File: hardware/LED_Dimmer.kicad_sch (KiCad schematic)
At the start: 20 parts, among them J1 Molex PicoBlade 53261-0871 1x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, J2 PicoBlade_510210800_1x08, M1 500798001, M2 500798001, M3 500798001, M4 500798001, M5 500798001, M6 500798001, M7 500798001, M8 500798001, Q1 2N7002K-7, Q2 2N7002K-7, Q3 2N7002K-7, U1 BGM220P, U2 L78L33A

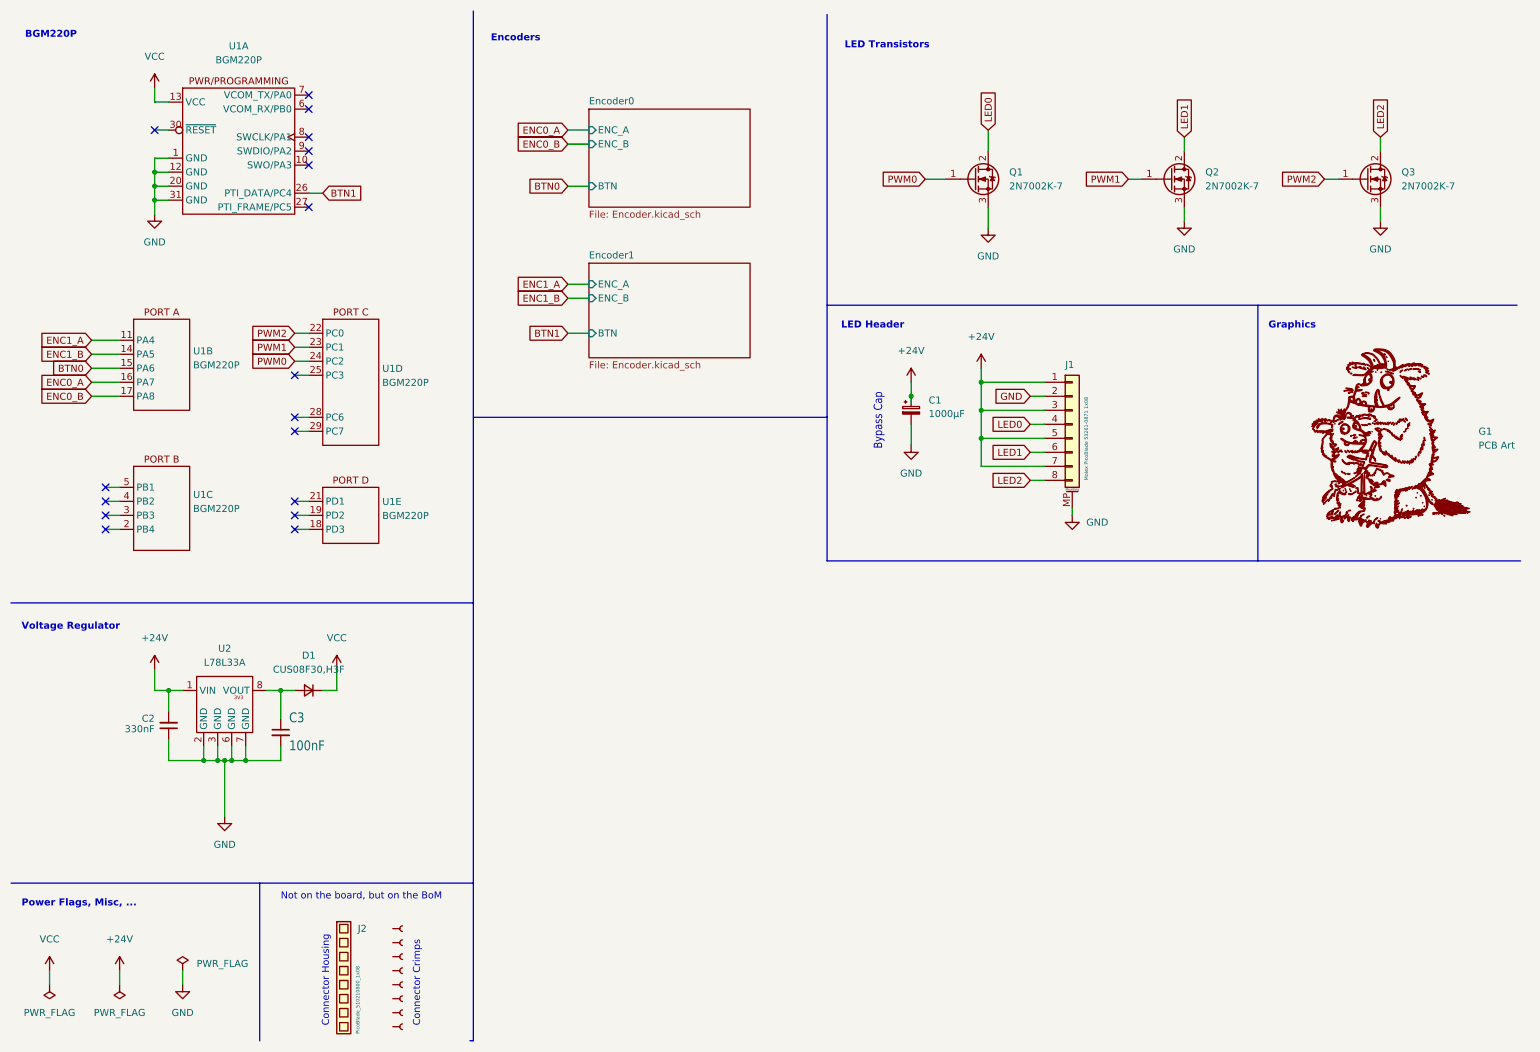
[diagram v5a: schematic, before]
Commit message: Updated to KiCad 9
- Changed LED Connectors to Kyocera
- Made board bigger
- Made art better and bigger
- Micro breakout now has header pins outside (easier to solder)
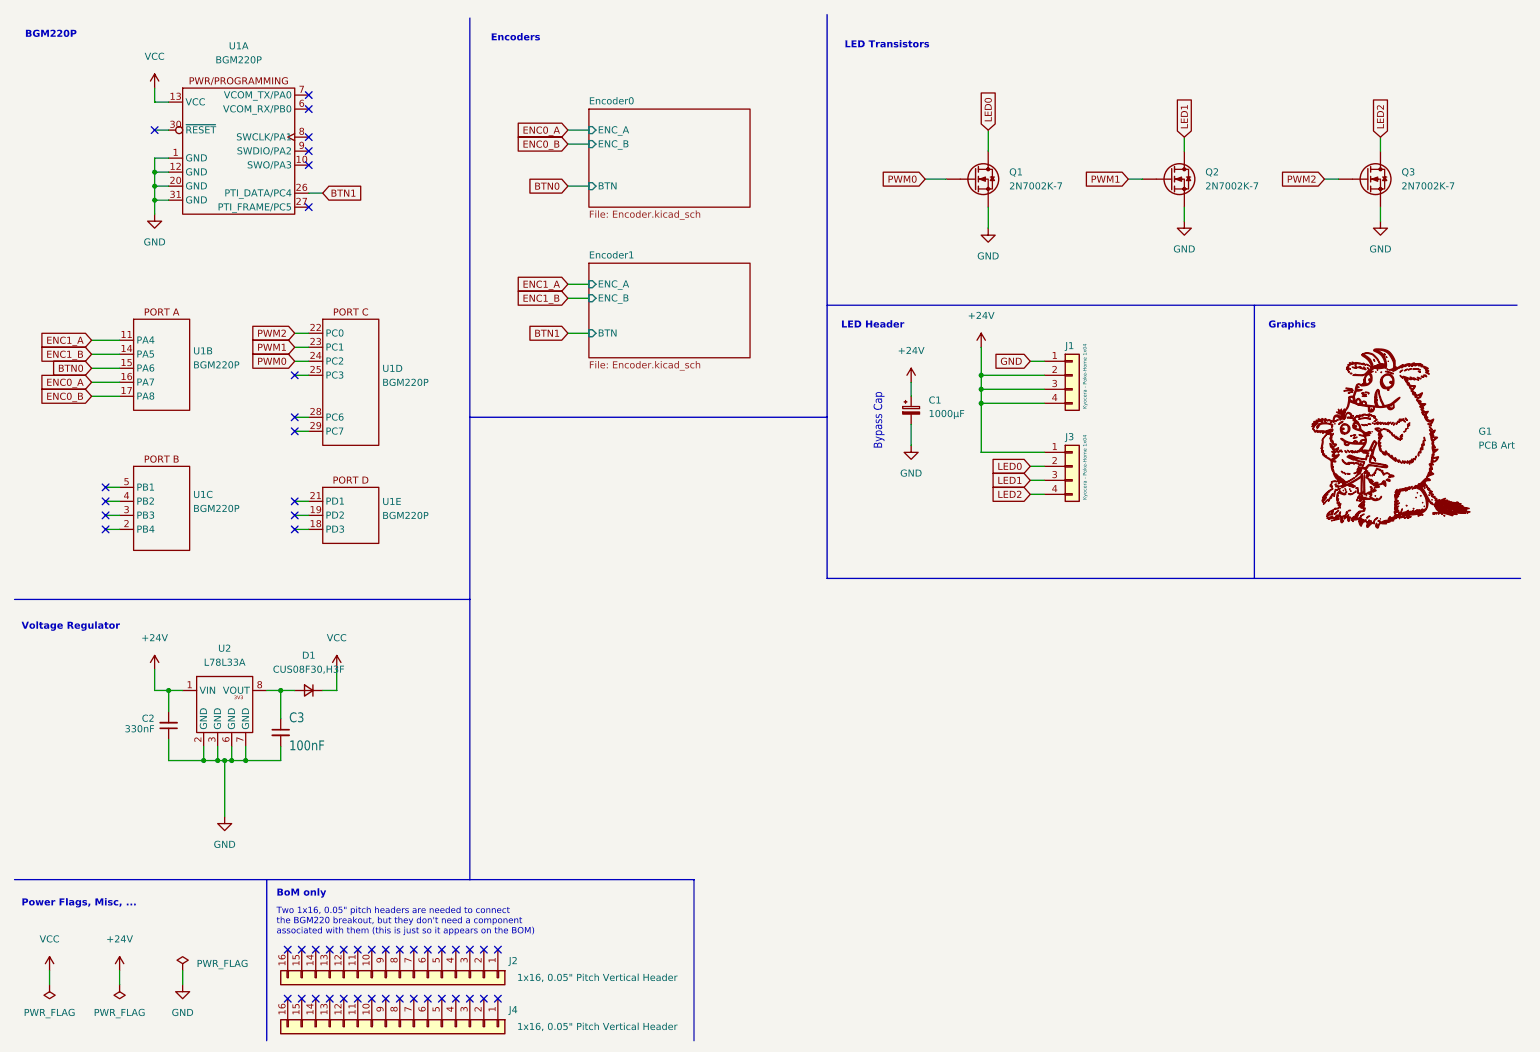
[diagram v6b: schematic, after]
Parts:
- removed J2: PicoBlade_510210800_1x08, symbol Gruffalo_Dimmer:PicoBlade_Housing_510210800_1x08
- removed M1, M2, M3, M4, M5, M6, M7, M8: 500798001, symbol Gruffalo_Dimmer:PicoBlade_Crimp_500798001_1x01
- added J2, J4: 1x16, 0.05" Pitch Vertical Header, symbol Connector_Generic:Conn_01x16
- added J3: Kyocera - Poke-Home 1x04, Gruffalo_Dimmer:Connector - Kyocera - Poke-Home 1x04 – Standard Horizontal 18-26 AWG, symbol Connector_Generic:Conn_01x04
- G1: footprint Gruffalo_Dimmer:Gruffalo_Art -> Gruffalo_Dimmer:Gruffalo_Art_42x47mm
- J1: value Molex PicoBlade 53261-0871 1x08 -> Kyocera - Poke-Home 1x04; footprint Gruffalo_Dimmer:Receptacle - Molex PicoBlade - SMD Right Angle 1x08 -> Gruffalo_Dimmer:Connector - Kyocera - Poke-Home 1x04 – Standard Horizontal 18-26 AWG; symbol Connector_Generic_MountingPin:Conn_01x08_MountingPin -> Connector_Generic:Conn_01x04; Comments Molex PicoBlade 1x08, SMD, Right Angle. Mates with P/N 5102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 -> Kyocera - Poke-Home 1x04 – Standard Horizontal 18-26 AWG; Digikey PN WM7626CT-ND -> (none); Farnell PN 1125376 -> (none); MPN 532610871 -> (none)
- Q1, Q2, Q3: symbol Device:Q_NMOS_GDS -> Device:Q_NMOS
- U1: footprint BGM220P_Breakout:BGM220P_Header_SMD -> BGM220P_Breakout:BGM220P_Header_SMD_Out
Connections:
- net +24V: now also J1.2 (Pin_2), J1.4 (Pin_4), J3.1 (Pin_1); no longer J1.1 (Pin_1), J1.5 (Pin_5), J1.7 (Pin_7)
- net GND: now also J1.1 (Pin_1), Q1.S, Q2.S, Q3.S; no longer J1.2 (Pin_2), J1.MP (MountPin), Q1.3 (S), Q2.3 (S), Q3.3 (S)
- net LED0: now also Q1.D, J3.2 (Pin_2); no longer J1.4 (Pin_4), Q1.2 (D)
- net LED1: now also Q2.D, J3.3 (Pin_3); no longer J1.6 (Pin_6), Q2.2 (D)
- net LED2: now also Q3.D, J3.4 (Pin_4); no longer J1.8 (Pin_8), Q3.2 (D)
- net PWM0: now also Q1.G; no longer Q1.1 (G)
- net PWM1: now also Q2.G; no longer Q2.1 (G)
- net PWM2: now also Q3.G; no longer Q3.1 (G)
- no-connect marks 17 -> 49
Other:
- note added: "BoM only"
- note added: "Two 1x16, 0.05" pitch headers are needed to connect the BGM220 breakout, but they don't need a component associated with them (this is just so it appears on the BOM)"
- note removed: "Connector Crimps"
- note removed: "Connector Housing"
- note removed: "Not on the board, but on the BoM"

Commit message: KiBot Config Udpdated to KiCad9
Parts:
- G1, J2, J4: Digikey PN (none) -> -; Farnell PN (none) -> -; MPN (none) -> -; Manufacturer (none) -> -
- J1, J3: Digikey PN (none) -> 478-009276004021906CT-ND; Farnell PN (none) -> 1891140; MPN (none) -> 009276004021906; Manufacturer Molex -> Kyocera
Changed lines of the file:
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@@
+			)
+		)
+		(property "Digikey PN" "-"
+			(at 82.55 195.58 90)
+			(effects
+				(font
+					(size 1.27 1.27)
+				)
+				(hide yes)
+			)
+		)
+		(property "Farnell PN" "-"
+			(at 82.55 195.58 90)
+			(effects
+				(font
+					(size 1.27 1.27)
+				)
+				(hide yes)
+			)
+		)
+		(property "MPN" "-"
+			(at 82.55 195.58 90)
+			(effects
+				(font
+					(size 1.27 1.27)
+				)
+				(hide yes)
+			)
+		)
+		(property "Manufacturer" "-"
+			(at 82.55 195.58 90)
+			(effects
+				(font
+					(size 1.27 1.27)
+				)
+				(hide yes)
 			)
 		)
@@
 			)
 		)
-		(property "Datasheet" "~"
+		(property "Datasheet" "https://datasheets.kyocera-avx.com/PokeHomeHorizontal_00-9276.pdf"
 			(at 204.47 77.47 0)
 			(effects
@@
 			)
 		)
-		(property "Digikey PN" ""
+		(property "Digikey PN" "478-009276004021906CT-ND"
 			(at 204.47 77.47 0)
 			(effects
@@
 			)
 		)
-		(property "Farnell PN" ""
+		(property "Farnell PN" "1891140"
 			(at 204.47 77.47 0)
 			(effects
@@
 			)
 		)
-		(property "MPN" ""
+		(property "MPN" "009276004021906"
 			(at 204.47 77.47 0)
 			(effects
@@
 			)
 		)
-		(property "Manufacturer" "Molex"
+		(property "Manufacturer" "Kyocera"
 			(at 204.47 77.47 0)
 			(effects
@@
 			)
 		)
-		(property "Datasheet" "~"
+		(property "Datasheet" "https://datasheets.kyocera-avx.com/PokeHomeHorizontal_00-9276.pdf"
 			(at 204.47 93.98 0)
 			(effects
@@
 			)
 		)
-		(property "Digikey PN" ""
+		(property "Digikey PN" "478-009276004021906CT-ND"
 			(at 204.47 93.98 0)
 			(effects
@@
 			)
 		)
-		(property "Farnell PN" ""
+		(property "Farnell PN" "1891140"
 			(at 204.47 93.98 0)
 			(effects
@@
 			)
 		)
-		(property "MPN" ""
+		(property "MPN" "009276004021906"
 			(at 204.47 93.98 0)
 			(effects
@@
 			)
 		)
-		(property "Manufacturer" "Molex"
+		(property "Manufacturer" "Kyocera"
 			(at 204.47 93.98 0)
 			(effects
@@
 			)
 		)
+		(property "Digikey PN" "-"
+			(at 82.55 186.69 90)
+			(effects
+				(font
+					(size 1.27 1.27)
+				)
+				(hide yes)
+			)
+		)
+		(property "Farnell PN" "-"
+			(at 82.55 186.69 90)
+			(effects
+				(font
+					(size 1.27 1.27)
+				)
+				(hide yes)
+			)
+		)
+		(property "MPN" "-"
+			(at 82.55 186.69 90)
+			(effects
+				(font
+					(size 1.27 1.27)
+				)
+				(hide yes)
+			)
+		)
+		(property "Manufacturer" "-"
+			(at 82.55 186.69 90)
+			(effects
+				(font
+					(size 1.27 1.27)
+				)
+				(hide yes)
+			)
+		)
 		(pin "6"
 		)
@@
 			)
 		)
-		(property "Datasheet" ""
+		(property "Datasheet" "~"
 			(at 262.255 88.9 0)
 			(effects
@@
 			)
 		)
+		(property "Digikey PN" "-"
+			(at 262.255 88.9 0)
+			(effects
+				(font
+					(size 1.27 1.27)
+				)
+				(hide yes)
+			)
+		)
+		(property "Farnell PN" "-"
+			(at 262.255 88.9 0)
+			(effects
+				(font
+					(size 1.27 1.27)
+				)
+				(hide yes)
+			)
+		)
+		(property "MPN" "-"
+			(at 262.255 88.9 0)
+			(effects
+				(font
+					(size 1.27 1.27)
+				)
+				(hide yes)
+			)
+		)
+		(property "Manufacturer" "-"
+			(at 262.255 88.9 0)
+			(effects
+				(font
+					(size 1.27 1.27)
+				)
+				(hide yes)
+			)
+		)

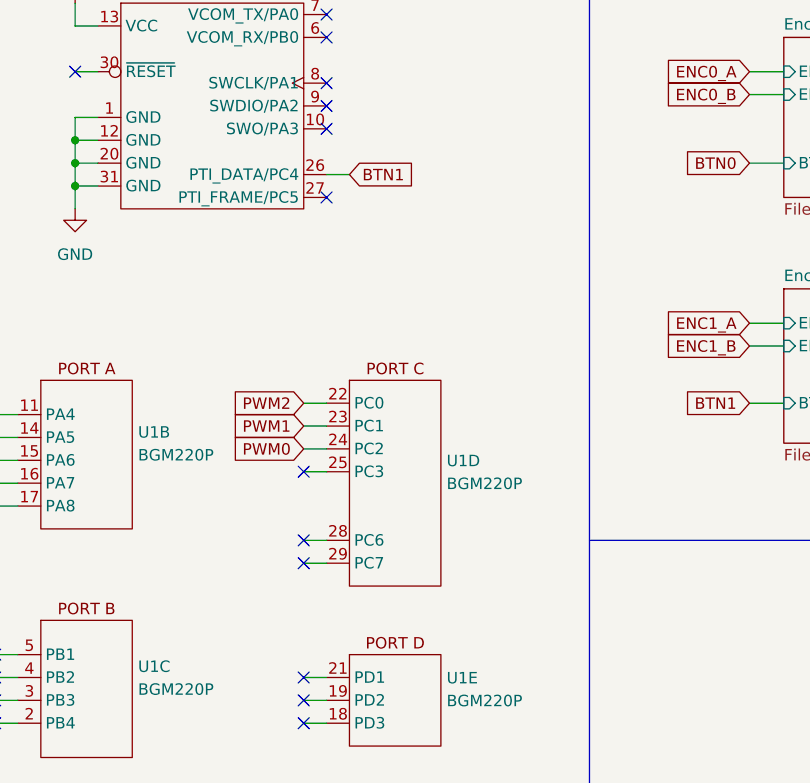
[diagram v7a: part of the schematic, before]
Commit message: Connected buttons to EM4 wake up pins
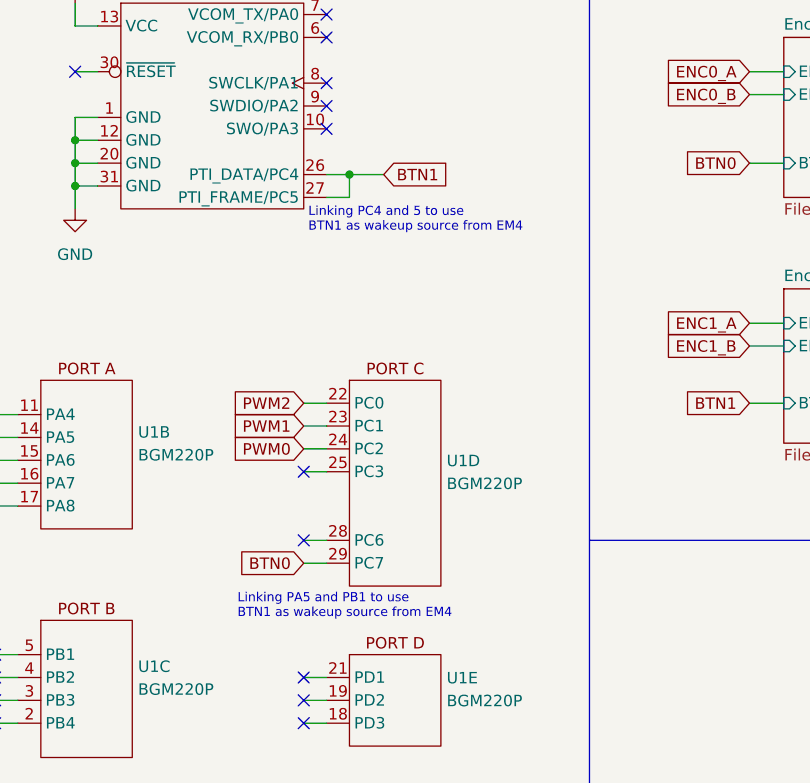
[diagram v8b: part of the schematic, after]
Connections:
- net BTN0: now also U1.29 (PC7)
- net BTN1: now also U1.27 (PTI_FRAME/PC5)
- no-connect marks 49 -> 47
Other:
- note added: "Linking PA5 and PB1 to use BTN1 as wakeup source from EM4"
- note added: "Linking PC4 and 5 to use BTN1 as wakeup source from EM4"
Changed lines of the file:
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@@
+		)
+	)
+	(text "Linking PC4 and 5 to use\nBTN1 as wakeup source from EM4"
+		(exclude_from_sim no)
+		(at 64.008 49.53 0)
+		(effects
+			(font
+				(size 1.016 1.016)
+			)
+			(justify left)
 		)
 	)
@@
 			)
 			(justify right bottom)
+		)
+	)
+	(text "Linking PA5 and PB1 to use\nBTN1 as wakeup source from EM4"
+		(exclude_from_sim no)
+		(at 56.134 92.456 0)
+		(effects
+			(font
+				(size 1.016 1.016)
+			)
+			(justify left)
 		)
 	)
@@
 	)
 	(junction
+		(at 68.58 44.45)
+		(diameter 0)
+		(color 0 0 0 0)
+	)
+	(junction
 		(at 187.96 82.55)
 		(diameter 0)
@@
 	)
 	(no_connect
-		(at 66.04 46.99)
-	)
-	(no_connect
 		(at 66.04 29.21)
 	)
@@
 	)
 	(no_connect
-		(at 63.5 87.63)
+		(at 29.21 97.79)
 	)
 	(no_connect
@@
 	)
 	(no_connect
-		(at 29.21 97.79)
-	)
-	(no_connect
 		(at 29.21 100.33)
 	)
@@
 	(wire
 		(pts
+			(xy 68.58 46.99) (xy 68.58 44.45)
+		)
+		(stroke
+			(width 0)
+			(type default)
+		)
+	)
+	(wire
+		(pts
 			(xy 63.5 105.41) (xy 66.04 105.41)
 		)
@@
 	(wire
 		(pts
+			(xy 68.58 44.45) (xy 72.39 44.45)
+		)
+		(stroke
+			(width 0)
+			(type default)
+		)
+	)
+	(wire
+		(pts
 			(xy 63.5 77.47) (xy 66.04 77.47)
 		)
@@
 	(wire
 		(pts
+			(xy 66.04 46.99) (xy 68.58 46.99)
+		)
+		(stroke
+			(width 0)
+			(type default)
+		)
+	)
+	(wire
+		(pts
 			(xy 214.63 41.91) (xy 217.17 41.91)
 		)
@@
 	(global_label "BTN1"
 		(shape input)
-		(at 68.58 44.45 0)
+		(at 72.39 44.45 0)
 		(fields_autoplaced yes)
 		(effects
@@
 		)
 		(property "Intersheetrefs" "${INTERSHEET_REFS}"
-			(at 75.7707 44.5294 0)
+			(at 79.5807 44.5294 0)
 			(effects
 				(font
@@
 			(effects
 				(font
+					(size 1.27 1.27)
+				)
+				(justify right)
+				(hide yes)
+			)
+		)
+	)
+	(global_label "BTN0"
+		(shape input)
+		(at 63.5 87.63 180)
+		(fields_autoplaced yes)
+		(effects
+			(font
+				(size 1.27 1.27)
+			)
+			(justify right)
+		)
+		(property "Intersheetrefs" "${INTERSHEET_REFS}"
+			(at 56.3093 87.5506 0)
+			(effects
+				(font
